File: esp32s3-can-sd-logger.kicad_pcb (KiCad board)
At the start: 4 copper layers, 98 x 100 mm, 164 parts, among them J1 CAN1 + power harness, J10 Spare diff in, J2 Aux bus harness, J3 DevKit J1, J4 DevKit J3, J5 I2C / Qwiic, J6 WS2812, J7 Rail break-out, J8 microSD push-pull, J9 Sensor harness, Q1 DMG2301L, Q2 2N7002, Q3 2N7002, U1 TLV431A, U2 74AHCT1G125, U3 SRV05-4, U4 SRV05-4, U5 TJA1051T/3, U6 MCP2518FD, U7 TJA1051T/3, U8 ADS1115 (0x48), U9 ADS1115 (0x49), Y1 40MHz

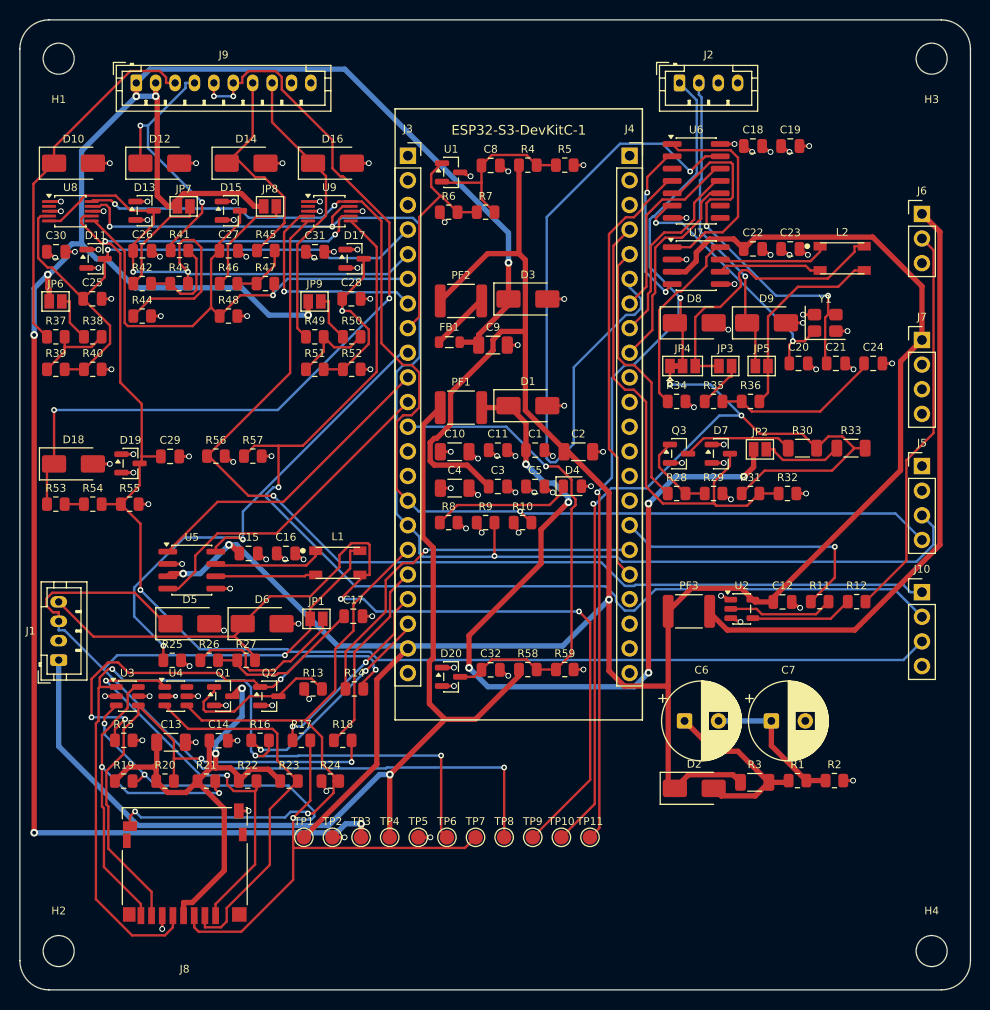
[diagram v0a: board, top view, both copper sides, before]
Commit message: microSD: turn the socket round so the card can actually go in
You called it: the slot was backwards. The tell is the solder joints --
a microSD goes in contacts-first, so the spring contacts and the tails
that solder to pads 1-8 are at the BACK of the slot and the mouth is at
the far end. Those pads sit at footprint y +5.35, so at 0 degrees the
mouth faced -y: into the middle of the board. The card could only have
been inserted from inside the laminate.

I read the U-shaped fab-layer outline on the pad side as the card the
first time round. It is not the card, it is the contact block.

J8 rotated to 180, mouth 8.5 mm from the bottom edge, and the board
re-routed around the moved pads: 0 violations, 0 unconnected.

audit_pcb gains check 7, which measures this instead of trusting the
eye. Nothing else could catch it -- the netlist is identical either
way and DRC has no opinion about which way a connector faces.

Fab files, plots and renders regenerated.

Co-Authored-By: Claude Opus 5 (1M context) <noreply@anthropic.com>
Claude-Session: https://claude.ai/code/session_01ApFXVTCuM7f3jNDae3R3qM
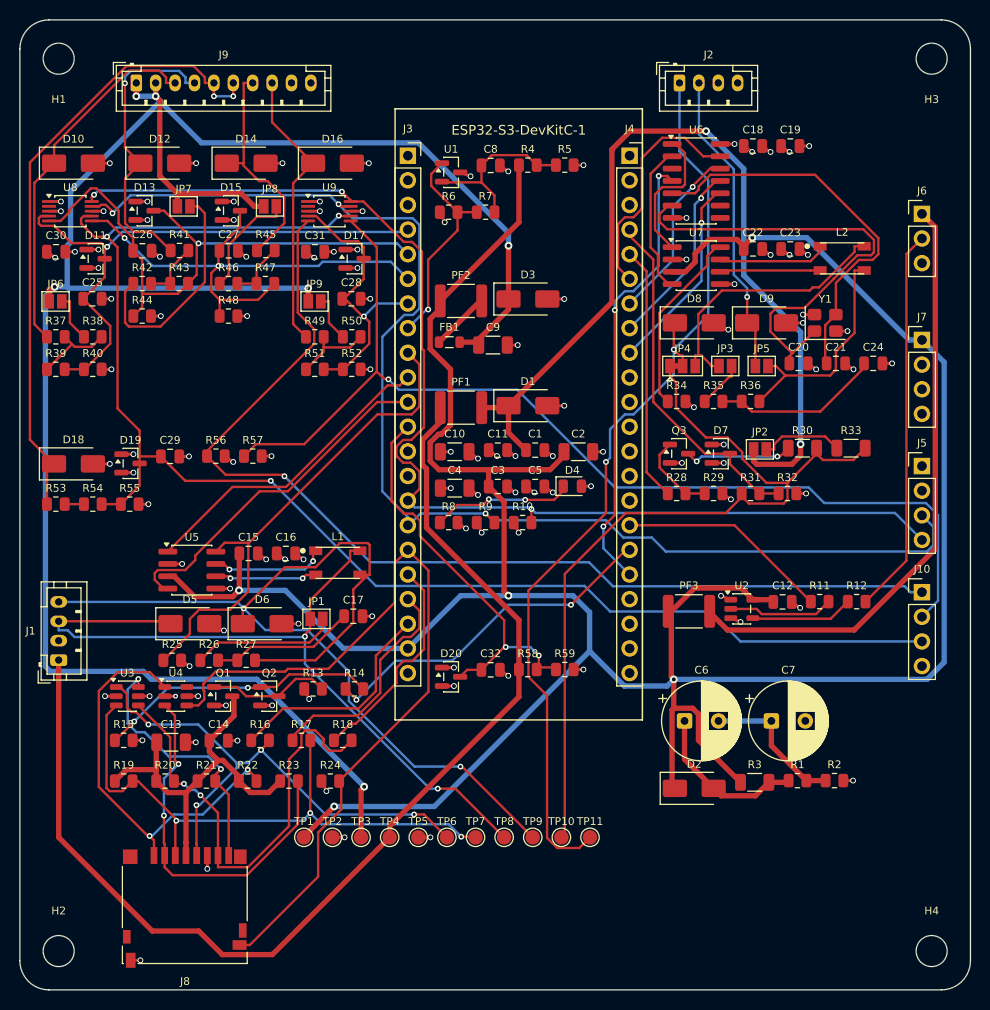
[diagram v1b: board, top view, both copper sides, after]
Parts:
- JP1: value TERM (default OFF) -> TERM
- JP2: value KPU (default OFF) -> KPU
- JP3: value TERM2 (default OFF) -> TERM2
- JP4: value AUXSEL (default K-line) -> AUXSEL
- JP5: value AUXCL (default OFF) -> AUXCL
- moved J8 4.50 mm to (17.0, 91.5), turned to 180 degrees
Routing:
- net CAN2_CS: track 72.3 -> 24.2 mm, vias 1 -> 0
- net SD_CLK_C: track 90.3 -> 55.2 mm, vias 3 -> 4
- net CAN_H: track 111.4 -> 80.8 mm
- net +5V: track 286.6 -> 309.3 mm, vias 3 -> 5
- net SENS_RTN: track 87.8 -> 65.5 mm, vias 4 -> 2
- net XTAL1: track 27.4 -> 49.3 mm, vias 2 -> 0
- net SD_CMD_C: track 81.0 -> 61.8 mm
- net +5VS: track 236.1 -> 218.9 mm, vias 8 -> 6
- net SD_EN_G: track 46.0 -> 29.0 mm, vias 4 -> 2
- net SD_VDD: track 55.9 -> 40.2 mm, vias 2 -> 0
- net SD_CD: track 67.7 -> 83.4 mm, vias 2 -> 0
- net SD_D1_C: track 41.6 -> 27.2 mm
- net K_RX: track 49.9 -> 36.2 mm
- net AIN2_PU: track 11.6 -> 23.6 mm
- net AIN4: track 41.5 -> 30.1 mm, vias 2 -> 1
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
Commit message: Space the parts for hand assembly: median gap 0.40 -> 1.20 mm
This board was laid out for an assembly house at a 0.4 mm courtyard gap.
It is being built by hand now, so the shelf packer runs at 1.2 mm and
several zones grew to absorb it.

  median nearest neighbour   0.40 -> 1.20 mm
  parts with a neighbour
  closer than 1.0 mm           85 -> 12 of 100
  closer than 0.6 mm                   2 of 100

Not the 2.5 mm the gate controller gets. That board carries half the
parts on the same area; here 2.5 wants about 1400 mm2 more copper, which
means growing past 100 mm and out of JLCPCB's cheap tier, and stretching
the CAN, SPI and microSD runs to pay for it. 1.2 fits the outline that
already exists.

Two limits found by measuring rather than assuming, both written into
the file so the next person does not re-derive them:

  * The gap is only guaranteed WITHIN a zone. Two zones whose rectangles
    touch can still put a part from each against the seam -- Q1 and R27
    came out at 0.00 mm across the sd/can1 boundary. Insetting every zone
    by half a gap fixes it in one line and was tried, but it costs 1.2 mm
    of width per zone and the analogue channels are 8.7 mm single-file
    columns that stop being able to pair a resistor with a diode. The sd
    zone moved down 1 mm instead, which fixes the one pair that touched.

  * The four channels cannot be spaced. At 8.7 mm on an 8.9 pitch they
    are 0.2 mm apart, which is where the closest remaining pair lives
    (a ch1 diode and a ch2 capacitor, 0.34 mm). Narrowing to buy the gap
    was tried at 8.5, 8.4 and 7.9: below 8.7 the column wraps to an extra
    row and 30 mm of height becomes 35.7. There is no more height either.
    Four channels properly spaced needs a board wider than 100 mm.

Nothing regressed. Routed 0 violations / 0 unconnected, 88 nets, ERC
clean, audit_routes still reports nothing flagged -- the CAN, SPI and
microSD runs survived the spreading -- and 128/128 BOM lines carry a
part number. The tw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
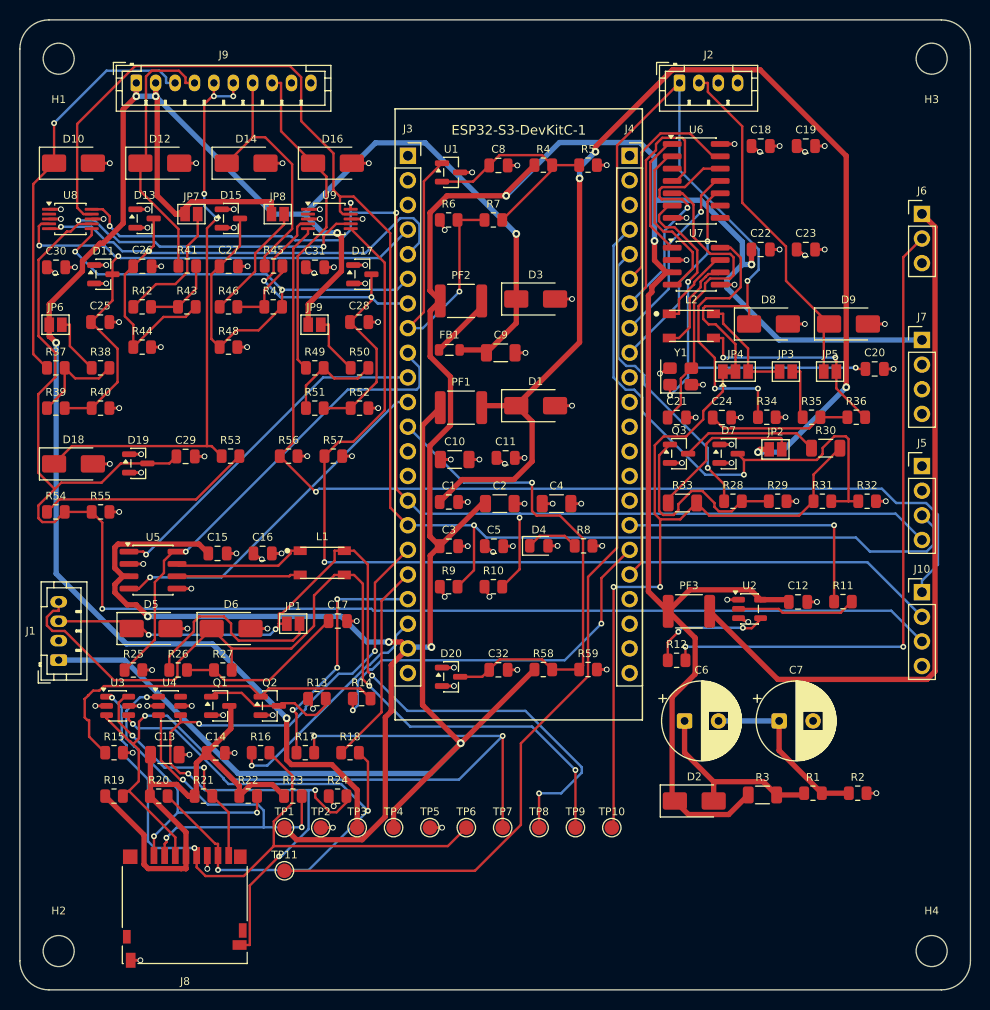
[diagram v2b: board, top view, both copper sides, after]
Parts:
- moved TP11 31.7 mm to (27.3, 87.7)
- moved R12 19.5 mm to (67.7, 66.0)
- moved R53 18.7 mm to (21.7, 45.0)
- moved R33 18.3 mm to (68.3, 49.8)
- moved C21 17.3 mm to (67.7, 41.0)
- moved L2 17.0 mm to (69.2, 31.6)
- moved C24 16.6 mm to (72.4, 41.0)
- moved Y1 15.9 mm to (68.1, 36.8)
- moved R8 14.1 mm to (58.1, 54.2)
- moved R36 11.0 mm to (86.2, 41.0)
- moved C4 10.6 mm to (55.3, 49.9)
- moved C1 10.4 mm to (44.2, 49.7)
- moved R35 10.2 mm to (81.6, 41.0)
- moved C2 9.71 mm to (49.5, 49.9)
- moved R34 9.44 mm to (77.0, 41.0)
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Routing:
- net AUX_A: track 98.4 -> 151.4 mm, vias 2 -> 1
- net SD_CMD_C: track 61.8 -> 94.7 mm
- net AGND_SENSE: track 151.3 -> 184.0 mm
- net OBD_VBAT_F: track 93.5 -> 121.3 mm, vias 2 -> 4
- net LED_DIN_J: track 39.8 -> 66.7 mm, vias 0 -> 2
- net I2C_SDA: track 133.2 -> 156.9 mm, vias 3 -> 1
- net K_RX: track 36.2 -> 58.3 mm, vias 0 -> 1
- net AGND_A: track 1.99 -> 22.2 mm
- net CAN2_H_C: track 28.6 -> 11.3 mm
- net SD_D0_C: track 47.0 -> 63.4 mm, vias 2 -> 3
- net SD_VDD: track 40.2 -> 53.9 mm
- net AIN4: track 30.1 -> 43.9 mm, vias 1 -> 2
- net K_TX_G: track 8.58 -> 21.7 mm
- net PWR_FAIL: track 22.8 -> 35.6 mm
- net LED_5V: track 62.7 -> 74.2 mm
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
